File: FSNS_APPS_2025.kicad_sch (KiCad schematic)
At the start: 16 parts, among them J1 Conn_01x04_Pin, U1 STM32F103C8Tx, Y1 16MHz

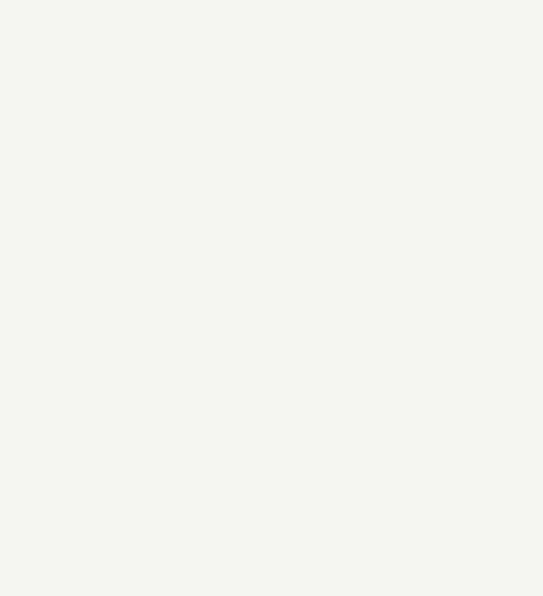
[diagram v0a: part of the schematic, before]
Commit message: Added LTSpice model for analog input stage
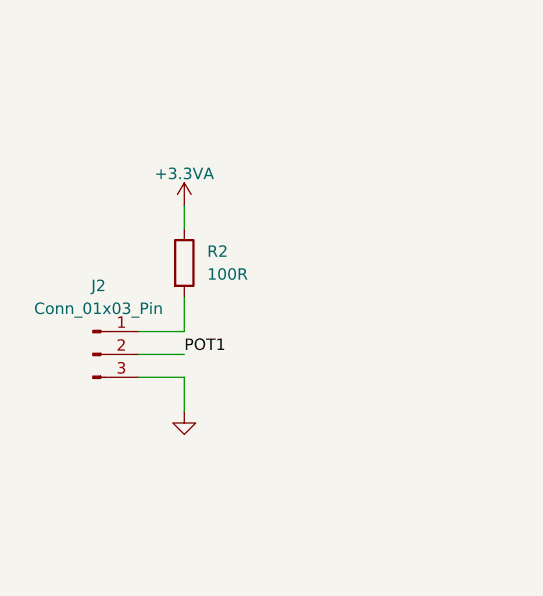
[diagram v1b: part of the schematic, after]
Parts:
- added J2: Conn_01x03_Pin, symbol Connector:Conn_01x03_Pin
- added R2: 100R, symbol Device:R
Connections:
- net +3.3VA: now also R2.1
- net GND: now also J2.3 (Pin_3)
- new net: J2.1 (Pin_1), R2.2
- new net POT1: J2.2 (Pin_2)

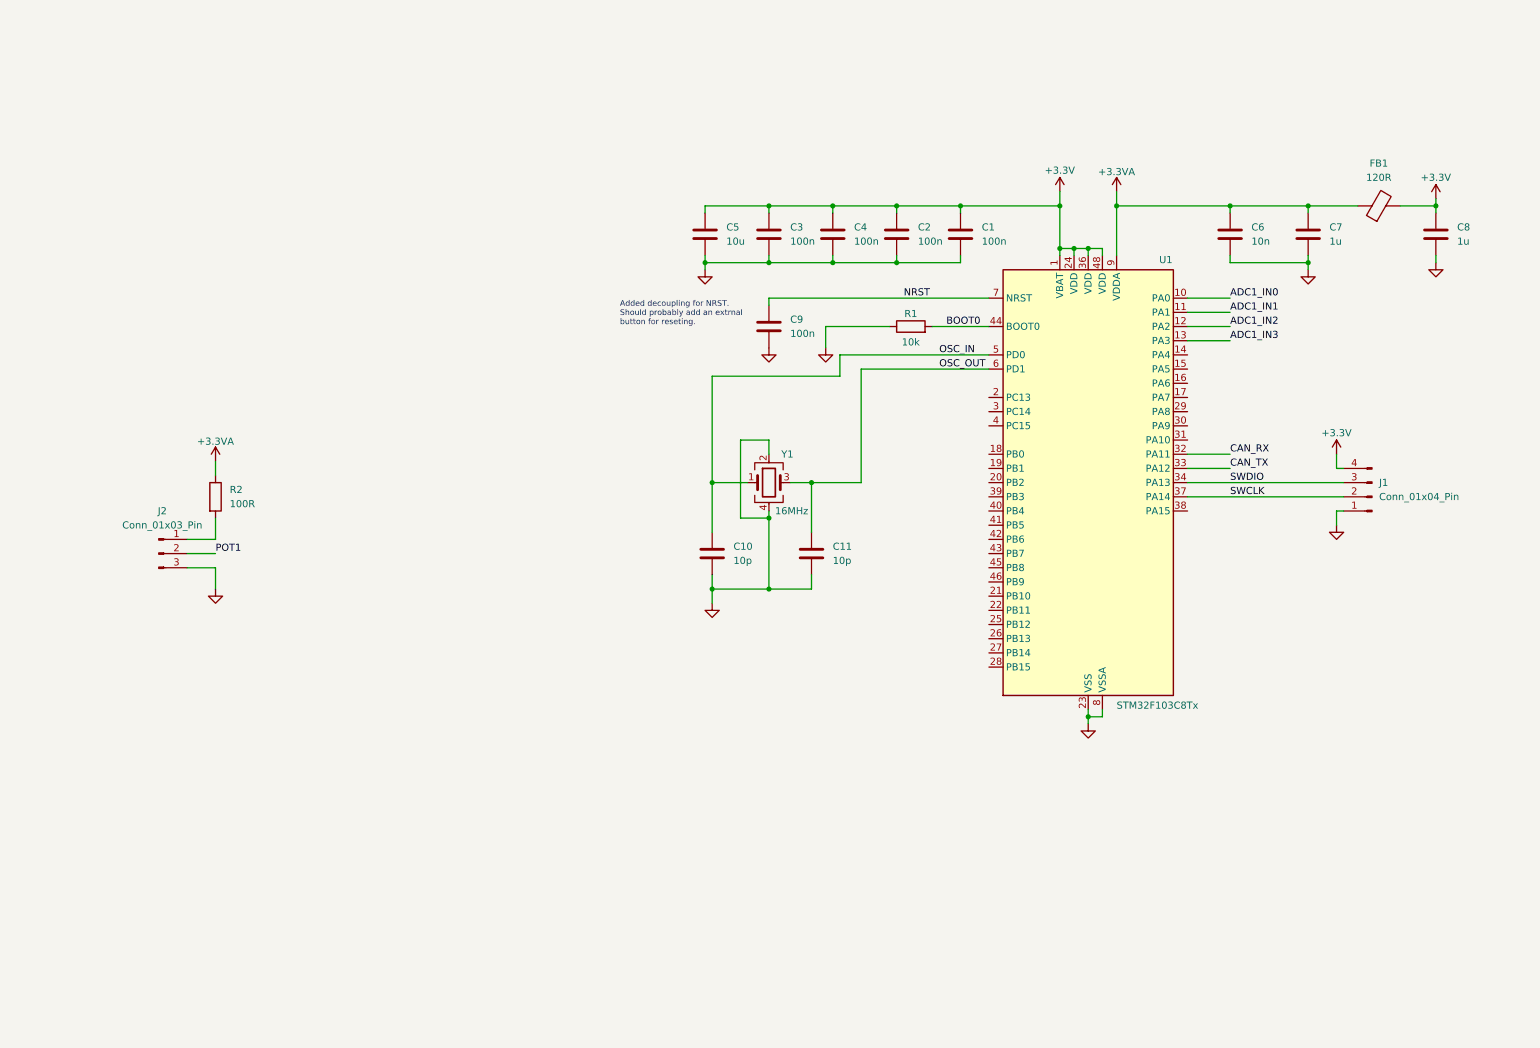
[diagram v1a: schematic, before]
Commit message: Added analog signal conditioning to schematic. AddedAPPS System FBD.
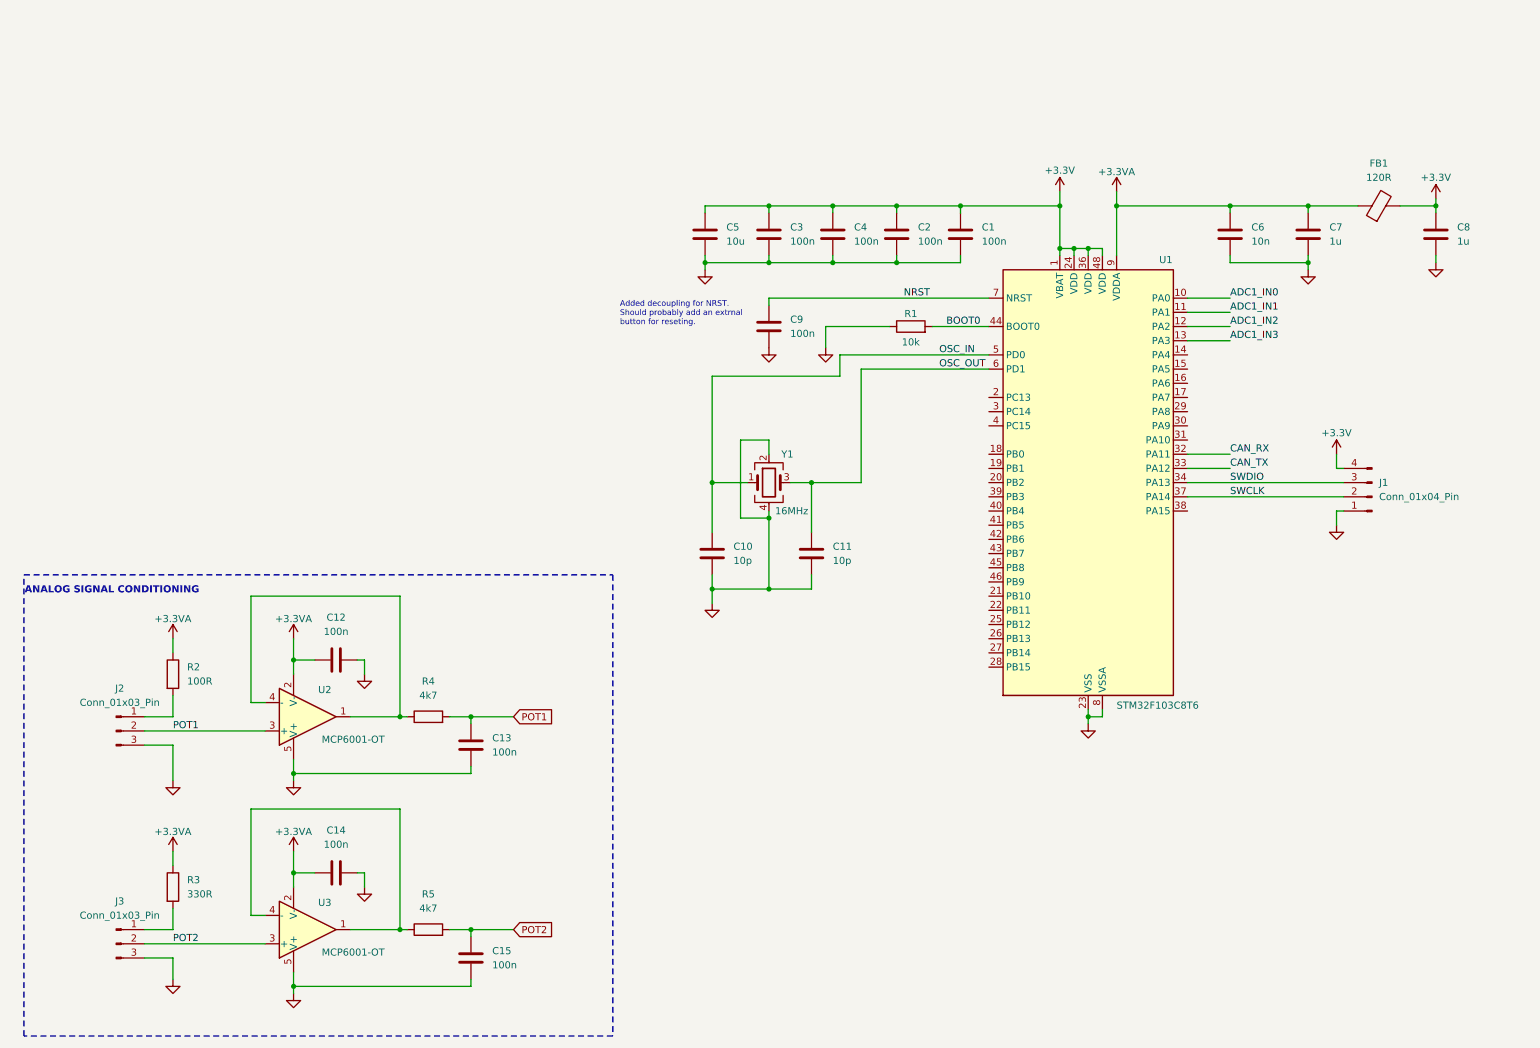
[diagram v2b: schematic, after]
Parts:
- added C12, C13, C14, C15: 100n, symbol Device:C
- added J3: Conn_01x03_Pin, symbol Connector:Conn_01x03_Pin
- added R3: 330R, symbol Device:R
- added R4, R5: 4k7, symbol Device:R
- added U2, U3: MCP6001-OT, Package_TO_SOT_SMD:SOT-23-5, symbol Amplifier_Operational:MCP6001-OT
- U1: value STM32F103C8Tx -> STM32F103C8T6
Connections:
- net +3.3VA: now also C12.1, C14.1, R3.1, U2.2 (V-), U3.2 (V-)
- net GND: now also C12.2, C13.1, C14.2, C15.1, J3.3 (Pin_3), U2.5 (V+), U3.5 (V+)
- net POT1: now also C13.2, R4.2, U2.3 (+)
- new net: R5.1, U3.1, U3.4 (-)
- new net: R4.1, U2.1, U2.4 (-)
- new net: J3.1 (Pin_1), R3.2
- new net POT2: C15.2, J3.2 (Pin_2), R5.2, U3.3 (+)
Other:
- note added: "ANALOG SIGNAL CONDITIONING"
- moved on the sheet: J2, R2

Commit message: Added a few components.
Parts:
- added C16, C18, C20: 1u, symbol Device:C
- added C17, C19, C21: 2.2u, symbol Device:C
- added C22: 100n, symbol Device:C
- added D1, D2: D_TVS, symbol Device:D_TVS
- added JP1: Jumper, symbol Jumper:Jumper_2_Small_Open
- added R3: 120R, symbol Device:R
- added U4, U5, U6: LM1117-Q1, Package_TO_SOT_SMD:SOT-223-3_TabPin2, symbol TI_Linear_regulator:LM1117-Q1_18V_1A
- added U7: TCAN3404-Q1, Package_SO:SOIC-8-1EP_3.9x4.9mm_P1.27mm_EP2.95x4.9mm_Mask2.71x3.4mm, symbol TCAN340x:TCAN340x
- renumbered R2 to R_B1, R3 to R_B2
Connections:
- net +3.3V: now also C17.1, C22.1, U4.2 (OUT), U7.3 (VCC)
- net +3.3VA: no longer R_B1.1, R_B2.1
- net CAN_RX: now also U7.4 (RXD)
- net CAN_TX: now also U7.1 (TXD)
- net GND: now also C16.2, C17.2, C18.2, C19.2, C20.2, C21.2, C22.2, D1.1 (A1), D2.1 (A1), U4.1 (GND), U5.1 (GND), U6.1 (GND), U7.2 (GND), U7.5 (SHDN/VIO), U7.8 (STB)
- net POT1: now also D1.2 (A2); no longer C13.2, R4.2
- net POT2: now also D2.2 (A2); no longer C15.2, R5.2
- new net: JP1.1 (A), R3.1
- new net +12V: C16.1, C18.1, C20.1, U4.3 (IN), U5.3 (IN), U6.3 (IN)
- new net +3.3V_POT1: C19.1, R_B1.1, U5.2 (OUT)
- new net +3.3V_POT2: C21.1, R_B2.1, U6.2 (OUT)
- new net APPS1_OUT: C13.2, R4.2
- new net APPS2_OUT: C15.2, R5.2
- new net CANH: JP1.2 (B), U7.7 (CANH)
- new net CANL: R3.2, U7.6 (CANL)
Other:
- note added: "CAN TRANSCEIVER"
- note added: "CONNECTORS"
- note added: "POWER"
- note added: "Place TVS diodes as close as possible to input pins."
- note added: "Place input and output capacitors as close to the device as possible. Use a ceramic output capacitor. Use LM111733QxxxRQ1."
- note added: "fc = 338Hz"
- moved on the sheet: C12, C13, C14, C15, J2, J3, R4, R5, R_B1, R_B2, U2, U3

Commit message: Finisished most of the schematic.
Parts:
- added C23: 1u, symbol Device:C
- added C24: 2.2u, symbol Device:C
- added D10, D11, D3, D4, D5, D6, D8, D9: LED, symbol Device:LED
- added D7: D, symbol Device:D
- added J4: Conn_01x02_Socket, symbol Connector:Conn_01x02_Socket
- added K1: PR12-12V-360-1A, PR12-12V-360-1A:RELAY_PR12-12V-360-1A, symbol PR12-12V-360-1A:PR12-12V-360-1A
- added Q1: NDT3055L, Package_TO_SOT_SMD:SOT-223-3_TabPin2, symbol Transistor_FET:NDT3055L
- added R10: 10K, symbol Device:R
- added R11, R12, R13, R14, R2, R6, R7, R8: 1K, symbol Device:R
- added R9: 100R, symbol Device:R
- added U8: LM1117-Q1, Package_TO_SOT_SMD:SOT-223-3_TabPin2, symbol TI_Linear_regulator:LM1117-Q1_18V_1A
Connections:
- net ADC1_IN0 is gone; now on net APPS1_OUT: U1.10 (PA0)
- net ADC1_IN1 is gone; now on net APPS2_OUT: U1.11 (PA1)
- net +12V: now also C23.1, J4.1 (Pin_1), U8.3 (IN)
- net +3.3V: now also R11.2, R2.2, R6.2, R7.2, R8.2
- net +3.3V_POT1: now also R12.2
- net +3.3V_POT2: now also R13.2
- net GND: now also C23.2, C24.2, D10.1 (K), D11.1 (K), D8.1 (K), D9.1 (K), J4.2 (Pin_2), Q1.3 (S), R10.2, U8.1 (GND)
- net PB0: now reaches U1.18 (PB0)
- net PB0: now also D3.1 (K)
- net PB1: now reaches U1.19 (PB1)
- net PB1: now also D4.1 (K)
- net PB2: now reaches U1.20 (PB2)
- net PB2: now also D5.1 (K)
- net PB3: now reaches U1.39 (PB3)
- net PB3: now also D6.1 (K)
- net RLY_EN: now reaches U1.40 (PB4)
- net RLY_EN: now also R9.1
- net ADC1_IN2: no longer names the net of U1.12 (PA2)
- net ADC1_IN3: no longer names the net of U1.13 (PA3)
- new net: D5.2 (A), R7.1
- new net: D9.2 (A), R12.1
- new net: D8.2 (A), R11.1
- new net: D11.2 (A), R14.1
- new net: D6.2 (A), R8.1
- new net: Q1.1 (G), R10.1, R9.2
- new net: D7.2 (A), K1.A2, Q1.2 (D)
- new net: D4.2 (A), R6.1
- new net: D3.2 (A), R2.1
- new net: D10.2 (A), R13.1
- new net +5V: C24.1, D7.1 (K), K1.A1, R14.2, U8.2 (OUT)
- no-connect marks 0 -> 24
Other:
- note added: "DEBUG LEDS"
- note added: "EXT. OSC."
- note added: "Place input and output capacitors as close to the device as possible. Use a ceramic output capacitor. Use LM111733QxxxRQ1 for 3.3V."
- note added: "SDC RELAY"
- note removed: "Place input and output capacitors as close to the device as possible. Use a ceramic output capacitor. Use LM111733QxxxRQ1."
- moved on the sheet: C1, C10, C11, C2, C3, C4, C5, C6, C7, C8, C9, FB1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

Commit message: Added a few PCB parts.
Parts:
- C1, C10, C11, C12, C13, C14, C15, C2, C3, C4, C6, C9: footprint (none) -> Capacitor_SMD:C_0402_1005Metric
- C16, C17, C18, C19, C20, C21, C22, C23, C24, C5, C7, C8: footprint (none) -> Capacitor_SMD:C_0603_1608Metric
- D10, D11, D3, D4, D5, D6, D8, D9: footprint (none) -> LED_SMD:LED_0603_1608Metric
- FB1: footprint (none) -> Inductor_SMD:L_0603_1608Metric
- R1, R11, R12, R13, R14, R2, R4, R5, R6, R7, R8, R_B1, R_B2: footprint (none) -> Resistor_SMD:R_0402_1005Metric
- R10, R9: footprint (none) -> Resistor_SMD:R_0603_1608Metric
- Y1: footprint (none) -> Crystal:Crystal_SMD_3225-4Pin_3.2x2.5mm
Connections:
- net GND: now also K1.COM
- net LED_DBG_3: now reaches U1.16 (PA6)
- net LED_DBG_3: now also D5.1 (K)
- net LED_DBG_4: now reaches U1.17 (PA7)
- net LED_DBG_4: now also D6.1 (K)
- net PB0 renamed LED_DBG_1
- net PB1 renamed LED_DBG_2
- net PB2: no longer names the net of U1.20 (PB2)
- net PB2: no longer D5.1 (K)
- net PB3: no longer names the net of U1.39 (PB3)
- net PB3: no longer D6.1 (K)

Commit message: Added mouting holes and test points.
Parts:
- added H1, H2, H3, H4: MountingHole_Pad, MountingHole:MountingHole_2.7mm_Pad, symbol Mechanical:MountingHole_Pad
- added SW1: SW_Push, symbol Switch:SW_Push
- added TP1, TP10, TP11, TP12, TP2, TP3, TP4, TP5, TP6, TP7, TP8, TP9: TestPoint, symbol Connector:TestPoint
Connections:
- net +3.3V: now also TP2.1
- net +3.3V_POT1: now also TP1.1
- net +3.3V_POT2: now also TP4.1
- net +5V: now also TP3.1
- net APPS1_OUT: now also TP7.1
- net APPS2_OUT: now also TP8.1
- net CANH: now also TP9.1
- net CANL: now also TP10.1
- net GND: now also H1.1, H2.1, H3.1, H4.1, SW1.1
- net NRST: now also SW1.2
- net POT1: now also TP5.1
- net POT2: now also TP6.1
- net at D7.2 (A), K1.A2, Q1.2 (D): now also TP12.1
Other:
- note added: "MOUNTING HOLES"
- note removed: "Added decoupling for NRST. Should probably add an extrnal button for reseting."
- moved on the sheet: C9
